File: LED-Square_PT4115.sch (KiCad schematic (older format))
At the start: 11 parts, among them U1 PT4115-SOT89-5

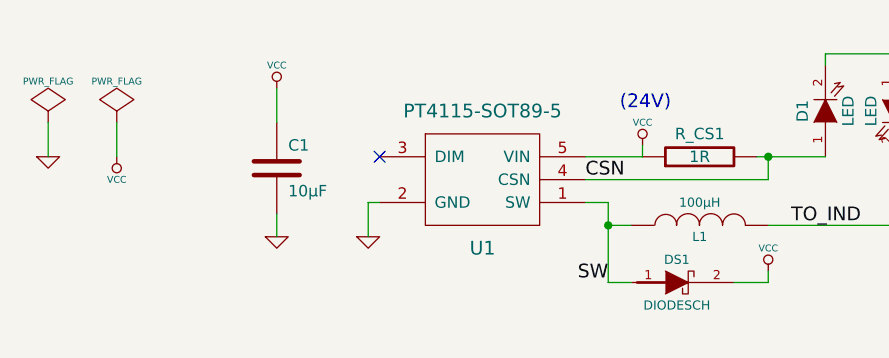
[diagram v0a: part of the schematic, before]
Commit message: Next step: add power connector(s) and maybe a pot for on-board dimming.
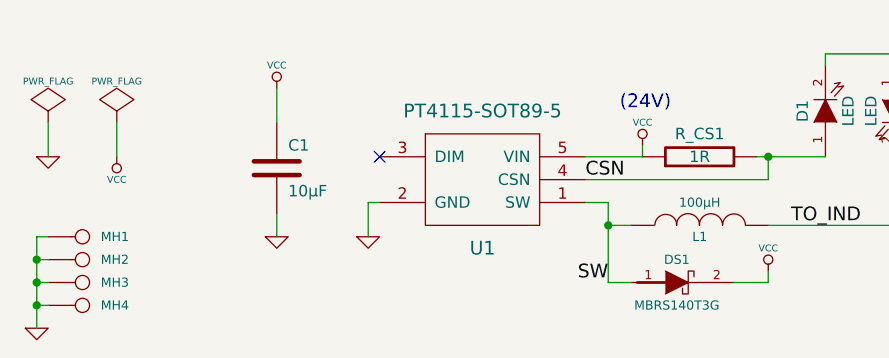
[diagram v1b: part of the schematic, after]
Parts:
- added MH1, MH2, MH3, MH4: CONN_1, symbol CONN_1
- DS1: value DIODESCH -> MBRS140T3G
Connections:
- net GND: now also MH1.1, MH2.1, MH3.1, MH4.1
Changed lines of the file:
@@
-EESchema Schematic File Version 2  date Fri 05 Oct 2012 10:36:36 PM CEST
+EESchema Schematic File Version 2  date Sat 06 Oct 2012 01:17:32 AM CEST
 LIBS:my_parts
 LIBS:power
@@
 Comment4 ""
 $EndDescr
-NoConn ~ 3100 2200
+$Comp
+L GND #PWR01
+U 1 1 506F6245
+P 1600 2950
+F 0 "#PWR01" H 1600 2950 30  0001 C CNN
+F 1 "GND" H 1600 2880 30  0001 C CNN
+	1    1600 2950
+	1    0    0    -1
+$EndComp
+Connection ~ 1600 2850
+Wire Wire Line
+	1600 2950 1600 2550
+Connection ~ 1600 2650
+Wire Wire Line
+	1600 2650 1650 2650
 Wire Wire Line
 	1950 2050 1950 2200
@@
 Wire Wire Line
 	1650 2050 1650 2200
+Wire Wire Line
+	1600 2850 1650 2850
+Wire Wire Line
+	1600 2550 1650 2550
+Wire Wire Line
+	1600 2750 1650 2750
+Connection ~ 1600 2750
+$Comp
+L CONN_1 MH4
+U 1 1 506F6221
+P 1800 2850
+F 0 "MH4" H 1880 2850 40  0000 L CNN
+F 1 "CONN_1" H 1800 2905 30  0001 C CNN
+	1    1800 2850
+	1    0    0    -1
+$EndComp
+$Comp
+L CONN_1 MH3
+U 1 1 506F621F
+P 1800 2750
+F 0 "MH3" H 1880 2750 40  0000 L CNN
+F 1 "CONN_1" H 1800 2805 30  0001 C CNN
+	1    1800 2750
+	1    0    0    -1
+$EndComp
+$Comp
+L CONN_1 MH2
+U 1 1 506F621C
+P 1800 2650
+F 0 "MH2" H 1880 2650 40  0000 L CNN
+F 1 "CONN_1" H 1800 2705 30  0001 C CNN
+	1    1800 2650
+	1    0    0    -1
+$EndComp
+$Comp
+L CONN_1 MH1
+U 1 1 506F6219
+P 1800 2550
+F 0 "MH1" H 1880 2550 40  0000 L CNN
+F 1 "CONN_1" H 1800 2605 30  0001 C CNN
+	1    1800 2550
+	1    0    0    -1
+$EndComp
+NoConn ~ 3100 2200
 Text Label 4900 2500 0    60   ~ 0
 TO_IND
@@
 White LEDs
 $Comp
-L VCC #PWR01
+L VCC #PWR02
 U 1 1 506F3B94
 P 1950 2200
-F 0 "#PWR01" H 1950 2300 30  0001 C CNN
+F 0 "#PWR02" H 1950 2300 30  0001 C CNN
 F 1 "VCC" H 1950 2300 30  0000 C CNN
 	1    1950 2200
@@
 $EndComp
 $Comp
-L GND #PWR02
+L GND #PWR03
 U 1 1 506F3B90
 P 1650 2200
-F 0 "#PWR02" H 1650 2200 30  0001 C CNN
+F 0 "#PWR03" H 1650 2200 30  0001 C CNN
 F 1 "GND" H 1650 2130 30  0001 C CNN
 	1    1650 2200
@@
 $EndComp
 $Comp
-L PWR_FLAG #FLG03
+L PWR_FLAG #FLG04
 U 1 1 506F3B8B
 P 1950 2050
-F 0 "#FLG03" H 1950 2145 30  0001 C CNN
+F 0 "#FLG04" H 1950 2145 30  0001 C CNN
 F 1 "PWR_FLAG" H 1950 2230 30  0000 C CNN
 	1    1950 2050
@@
 $EndComp
 $Comp
-L PWR_FLAG #FLG04
+L PWR_FLAG #FLG05
 U 1 1 506F3B82
 P 1650 2050
-F 0 "#FLG04" H 1650 2145 30  0001 C CNN
+F 0 "#FLG05" H 1650 2145 30  0001 C CNN
 F 1 "PWR_FLAG" H 1650 2230 30  0000 C CNN
 	1    1650 2050
@@
 $EndComp
 $Comp
-L VCC #PWR05
+L VCC #PWR06
 U 1 1 506F3B33
 P 4800 2700
-F 0 "#PWR05" H 4800 2800 30  0001 C CNN
+F 0 "#PWR06" H 4800 2800 30  0001 C CNN
 F 1 "VCC" H 4800 2800 30  0000 C CNN
 	1    4800 2700
@@
 $EndComp
 $Comp
-L VCC #PWR06
+L VCC #PWR07
 U 1 1 506F3A4D
 P 2650 1900
-F 0 "#PWR06" H 2650 2000 30  0001 C CNN
+F 0 "#PWR07" H 2650 2000 30  0001 C CNN
 F 1 "VCC" H 2650 2000 30  0000 C CNN
 	1    2650 1900
@@
 $EndComp
 $Comp
-L GND #PWR07
+L GND #PWR08
 U 1 1 506F3A48
 P 2650 2550
-F 0 "#PWR07" H 2650 2550 30  0001 C CNN
+F 0 "#PWR08" H 2650 2550 30  0001 C CNN
 F 1 "GND" H 2650 2480 30  0001 C CNN
 	1    2650 2550
@@
 $EndComp
 $Comp
-L VCC #PWR08
+L VCC #PWR09
 U 1 1 506F3A0F
 P 4250 2150
-F 0 "#PWR08" H 4250 2250 30  0001 C CNN
+F 0 "#PWR09" H 4250 2250 30  0001 C CNN
 F 1 "VCC" H 4250 2250 30  0000 C CNN
 	1    4250 2150
@@
 $EndComp
 $Comp
-L GND #PWR09
+L GND #PWR010
 U 1 1 506F39FF
 P 3050 2550
-F 0 "#PWR09" H 3050 2550 30  0001 C CNN
+F 0 "#PWR010" H 3050 2550 30  0001 C CNN
 F 1 "GND" H 3050 2480 30  0001 C CNN
 	1    3050 2550
@@
 P 4400 2750
 F 0 "DS1" H 4400 2850 40  0000 C CNN
-F 1 "DIODESCH" H 4400 2650 40  0000 C CNN
+F 1 "MBRS140T3G" H 4400 2650 40  0000 C CNN
 	1    4400 2750
 	1    0    0    -1

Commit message: Added copper pour as LED heatsinks.
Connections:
- net D1HS: now reaches D1.2 (K), D2.1 (A)
- net D2HS: now reaches D2.2 (K), D3.1 (A)
- net D3HS: now reaches D3.2 (K), D4.1 (A)
- net D4HS: now reaches D4.2 (K), D5.1 (A)
- net D5HS: now reaches D5.2 (K), D6.1 (A)
- net TO_IND renamed D6HS
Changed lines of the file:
@@
-EESchema Schematic File Version 2  date Sat 06 Oct 2012 01:17:32 AM CEST
+EESchema Schematic File Version 2  date Sat 06 Oct 2012 12:05:23 PM CEST
 LIBS:my_parts
 LIBS:power
@@
 Sheet 1 1
 Title "LED-Square PT4115"
-Date "5 oct 2012"
+Date "6 oct 2012"
 Rev "0.10"
 Comp "2012 - blog.spitzenpfeil.org"
@@
 Comment4 ""
 $EndDescr
+Text Label 6550 2250 2    60   ~ 0
+D6HS
+Text Label 6250 1750 2    60   ~ 0
+D5HS
+Text Label 5950 2250 2    60   ~ 0
+D4HS
+Text Label 5650 1750 2    60   ~ 0
+D3HS
+Text Label 5350 2250 2    60   ~ 0
+D2HS
+Text Label 5050 1750 2    60   ~ 0
+D1HS
 $Comp
 L GND #PWR01
@@
 $EndComp
 NoConn ~ 3100 2200
-Text Label 4900 2500 0    60   ~ 0
-TO_IND
 Text Label 4000 2300 0    60   ~ 0
 CSN
@@
 Text Notes 4150 2000 0    60   ~ 0
 (24V)
-Text Notes 5600 1700 0    60   ~ 0
+Text Notes 5550 1600 0    60   ~ 0
 White LEDs
 $Comp

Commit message: Added board-to-board connectors.
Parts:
- added P1: IN, symbol CONN_6
- added P2: OUT, symbol CONN_6
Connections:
- net GND: now also P1.1, P1.2, P2.5, P2.6; no longer MH1.1, MH2.1, MH3.1, MH4.1
- net VCC: now also P1.3, P1.4, P2.3, P2.4
- net DIM: now reaches U1.3 (DIM)
- net DIM: now also P1.6, P2.1
- no-connect marks 1 -> 6
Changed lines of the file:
@@
-EESchema Schematic File Version 2  date Sat 06 Oct 2012 12:05:23 PM CEST
+EESchema Schematic File Version 2  date Mon 22 Oct 2012 06:20:21 PM CEST
 LIBS:my_parts
 LIBS:power
@@
 Sheet 1 1
 Title "LED-Square PT4115"
-Date "6 oct 2012"
+Date "22 oct 2012"
 Rev "0.10"
 Comp "2012 - blog.spitzenpfeil.org"
@@
 Comment4 ""
 $EndDescr
+Connection ~ 2550 3450
+Wire Wire Line
+	2550 3450 2550 3550
+Wire Wire Line
+	2550 3550 2500 3550
+Connection ~ 2550 3650
+Wire Wire Line
+	2550 3650 2550 3750
+Wire Wire Line
+	2550 3750 2500 3750
+Wire Wire Line
+	2500 3950 2600 3950
+Wire Wire Line
+	1400 3950 1500 3950
+Wire Wire Line
+	1500 3750 1450 3750
+Connection ~ 1450 3650
+Wire Wire Line
+	1450 3750 1450 3650
+Connection ~ 1450 3450
+Wire Wire Line
+	1450 3450 1450 3550
+Wire Wire Line
+	1450 3550 1500 3550
+Wire Wire Line
+	1950 2050 1950 2200
+Connection ~ 4100 2500
+Wire Wire Line
+	4200 2750 4100 2750
+Wire Wire Line
+	4100 2750 4100 2400
+Wire Wire Line
+	6550 2200 6550 2500
+Wire Wire Line
+	6550 2500 4800 2500
+Connection ~ 4800 2200
+Wire Wire Line
+	5050 2200 4750 2200
+Wire Wire Line
+	2650 1900 2650 2050
+Wire Wire Line
+	4250 2150 4250 2200
+Wire Wire Line
+	4250 2200 4000 2200
+Wire Wire Line
+	6550 1800 6550 1750
+Wire Wire Line
+	6550 1750 6250 1750
+Wire Wire Line
+	6250 1750 6250 1800
+Wire Wire Line
+	5950 1800 5950 1750
+Wire Wire Line
+	5950 1750 5650 1750
+Wire Wire Line
+	5650 1750 5650 1800
+Wire Wire Line
+	5350 1800 5350 1750
+Wire Wire Line
+	5350 1750 5050 1750
+Wire Wire Line
+	5050 1750 5050 1800
+Wire Wire Line
+	5350 2200 5350 2250
+Wire Wire Line
+	5350 2250 5650 2250
+Wire Wire Line
+	5650 2250 5650 2200
+Wire Wire Line
+	5950 2200 5950 2250
+Wire Wire Line
+	5950 2250 6250 2250
+Wire Wire Line
+	6250 2250 6250 2200
+Wire Wire Line
+	3100 2400 3050 2400
+Wire Wire Line
+	3050 2400 3050 2550
+Wire Wire Line
+	4000 2300 4800 2300
+Wire Wire Line
+	4800 2300 4800 2200
+Wire Wire Line
+	2650 2450 2650 2550
+Wire Wire Line
+	4100 2400 4000 2400
+Wire Wire Line
+	4100 2500 4200 2500
+Wire Wire Line
+	4650 2750 4800 2750
+Wire Wire Line
+	4800 2750 4800 2700
+Wire Wire Line
+	1650 2050 1650 2200
+Wire Wire Line
+	1250 3500 1250 3450
+Wire Wire Line
+	1250 3450 1500 3450
+Wire Wire Line
+	1250 3700 1250 3650
+Wire Wire Line
+	1250 3650 1500 3650
+Wire Wire Line
+	3050 2200 3100 2200
+Wire Wire Line
+	2500 3650 2750 3650
+Wire Wire Line
+	2750 3650 2750 3700
+Wire Wire Line
+	2500 3450 2750 3450
+Wire Wire Line
+	2750 3450 2750 3500
+NoConn ~ 2500 3850
+NoConn ~ 1500 3850
+Text Label 2600 3950 0    60   ~ 0
+DIM
+Text Label 1400 3950 2    60   ~ 0
+DIM
+Text Label 3050 2200 2    60   ~ 0
+DIM
+$Comp
+L VCC #PWR?
+U 1 1 5085715F
+P 2750 3700
+F 0 "#PWR?" H 2750 3800 30  0001 C CNN
+F 1 "VCC" H 2750 3800 30  0000 C CNN
+	1    2750 3700
+	-1   0    0    1
+$EndComp
+$Comp
+L VCC #PWR?
+U 1 1 5085714E
+P 1250 3700
+F 0 "#PWR?" H 1250 3800 30  0001 C CNN
+F 1 "VCC" H 1250 3800 30  0000 C CNN
+	1    1250 3700
+	-1   0    0    1
+$EndComp
+$Comp
+L GND #PWR?
+U 1 1 50857132
+P 2750 3500
+F 0 "#PWR?" H 2750 3500 30  0001 C CNN
+F 1 "GND" H 2750 3430 30  0001 C CNN
+	1    2750 3500
+	1    0    0    -1
+$EndComp
+$Comp
+L GND #PWR?
+U 1 1 50857116
+P 1250 3500
+F 0 "#PWR?" H 1250 3500 30  0001 C CNN
+F 1 "GND" H 1250 3430 30  0001 C CNN
+	1    1250 3500
+	1    0    0    -1
+$EndComp
+$Comp
+L CONN_6 P2
+U 1 1 508570CC
+P 2150 3700
+F 0 "P2" V 2100 3700 60  0000 C CNN
+F 1 "OUT" V 2200 3700 60  0000 C CNN
+	1    2150 3700
+	-1   0    0    1
+$EndComp
+$Comp
+L CONN_6 P1
+U 1 1 508570C8
+P 1850 3700
+F 0 "P1" V 1800 3700 60  0000 C CNN
+F 1 "IN" V 1900 3700 60  0000 C CNN
+	1    1850 3700
+	1    0    0    -1
+$EndComp
+NoConn ~ 1650 2850
+NoConn ~ 1650 2750
+NoConn ~ 1650 2650
+NoConn ~ 1650 2550
 Text Label 6550 2250 2    60   ~ 0
 D6HS
@@
 D1HS
 $Comp
-L GND #PWR01
-U 1 1 506F6245
-P 1600 2950
-F 0 "#PWR01" H 1600 2950 30  0001 C CNN
-F 1 "GND" H 1600 2880 30  0001 C CNN
-	1    1600 2950
-	1    0    0    -1
-$EndComp
-Connection ~ 1600 2850
-Wire Wire Line
-	1600 2950 1600 2550
-Connection ~ 1600 2650
-Wire Wire Line
-	1600 2650 1650 2650
-Wire Wire Line
-	1950 2050 1950 2200
-Connection ~ 4100 2500
-Wire Wire Line
-	4200 2750 4100 2750
-Wire Wire Line
-	4100 2750 4100 2400
-Wire Wire Line
-	6550 2200 6550 2500
-Wire Wire Line
-	6550 2500 4800 2500
-Connection ~ 4800 2200
-Wire Wire Line
-	5050 2200 4750 2200
-Wire Wire Line
-	2650 1900 2650 2050
-Wire Wire Line
-	4250 2150 4250 2200
-Wire Wire Line
-	4250 2200 4000 2200
-Wire Wire Line
-	6550 1800 6550 1750
-Wire Wire Line
-	6550 1750 6250 1750
-Wire Wire Line
-	6250 1750 6250 1800
-Wire Wire Line
-	5950 1800 5950 1750
-Wire Wire Line
-	5950 1750 5650 1750
-Wire Wire Line
-	5650 1750 5650 1800
-Wire Wire Line
-	5350 1800 5350 1750
-Wire Wire Line
-	5350 1750 5050 1750
-Wire Wire Line
-	5050 1750 5050 1800
-Wire Wire Line
-	5350 2200 5350 2250
-Wire Wire Line
-	5350 2250 5650 2250
-Wire Wire Line
-	5650 2250 5650 2200
-Wire Wire Line
-	5950 2200 5950 2250
-Wire Wire Line
-	5950 2250 6250 2250
-Wire Wire Line
-	6250 2250 6250 2200
-Wire Wire Line
-	3100 2400 3050 2400
-Wire Wire Line
-	3050 2400 3050 2550
-Wire Wire Line
-	4000 2300 4800 2300
-Wire Wire Line
-	4800 2300 4800 2200
-Wire Wire Line
-	2650 2450 2650 2550
-Wire Wire Line
-	4100 2400 4000 2400
-Wire Wire Line
-	4100 2500 4200 2500
-Wire Wire Line
-	4650 2750 4800 2750
-Wire Wire Line
-	4800 2750 4800 2700
-Wire Wire Line
-	1650 2050 1650 2200
-Wire Wire Line
-	1600 2850 1650 2850
-Wire Wire Line
-	1600 2550 1650 2550
-Wire Wire Line
-	1600 2750 1650 2750
-Connection ~ 1600 2750
-$Comp
 L CONN_1 MH4
 U 1 1 506F6221
@@
 	1    0    0    -1
 $EndComp
-NoConn ~ 3100 2200
 Text Label 4000 2300 0    60   ~ 0
 CSN

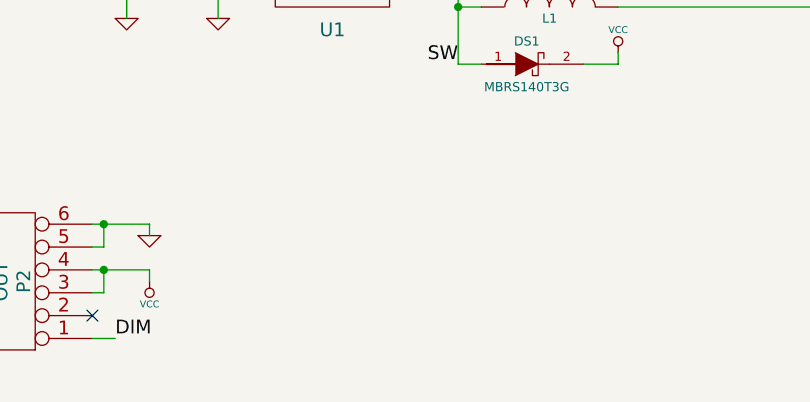
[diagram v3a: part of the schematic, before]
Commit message: Added a few more caps on the supply rail.
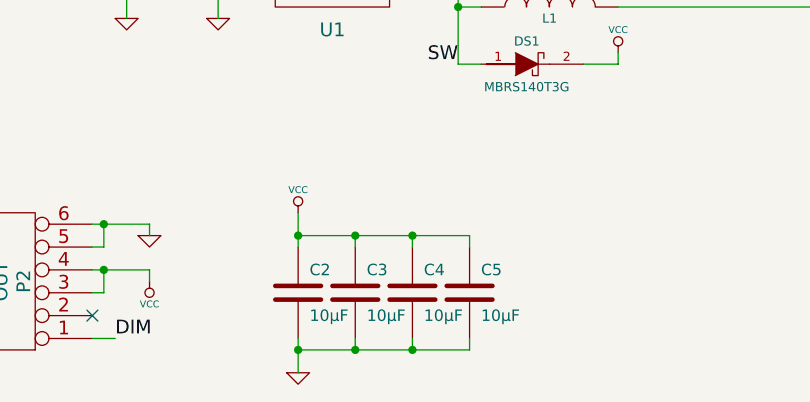
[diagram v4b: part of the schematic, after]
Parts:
- added C2, C3, C4, C5: 10µF, symbol C
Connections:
- net GND: now also C2.2, C3.2, C4.2, C5.2
- net VCC: now also C2.1, C3.1, C4.1, C5.1
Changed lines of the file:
@@
-EESchema Schematic File Version 2  date Mon 22 Oct 2012 06:20:21 PM CEST
+EESchema Schematic File Version 2  date Wed 24 Oct 2012 06:42:53 AM CEST
 LIBS:my_parts
 LIBS:power
@@
 Sheet 1 1
 Title "LED-Square PT4115"
-Date "22 oct 2012"
+Date "24 oct 2012"
 Rev "0.10"
 Comp "2012 - blog.spitzenpfeil.org"
@@
 Comment4 ""
 $EndDescr
+$Comp
+L VCC #PWR01
+U 1 1 508771C2
+P 3400 3400
+F 0 "#PWR01" H 3400 3500 30  0001 C CNN
+F 1 "VCC" H 3400 3500 30  0000 C CNN
+	1    3400 3400
+	1    0    0    -1
+$EndComp
+$Comp
+L GND #PWR02
+U 1 1 508771BD
+P 3400 4100
+F 0 "#PWR02" H 3400 4100 30  0001 C CNN
+F 1 "GND" H 3400 4030 30  0001 C CNN
+	1    3400 4100
+	1    0    0    -1
+$EndComp
+Connection ~ 3400 3500
+Wire Wire Line
+	3400 3400 3400 3550
+Connection ~ 3650 4000
+Wire Wire Line
+	3650 3950 3650 4000
+Wire Wire Line
+	4150 3950 4150 4000
+Wire Wire Line
+	4150 4000 3400 4000
+Connection ~ 3900 3500
+Wire Wire Line
+	3900 3550 3900 3500
 Connection ~ 2550 3450
 Wire Wire Line
@@
 Wire Wire Line
 	2750 3450 2750 3500
+Wire Wire Line
+	3400 3500 4150 3500
+Wire Wire Line
+	4150 3500 4150 3550
+Wire Wire Line
+	3650 3550 3650 3500
+Connection ~ 3650 3500
+Wire Wire Line
+	3900 3950 3900 4000
+Connection ~ 3900 4000
+Wire Wire Line
+	3400 4100 3400 3950
+Connection ~ 3400 4000
+$Comp
+L C C5
+U 1 1 50877174
+P 4150 3750
+F 0 "C5" H 4200 3850 50  0000 L CNN
+F 1 "10µF" H 4200 3650 50  0000 L CNN
+	1    4150 3750
+	1    0    0    -1
+$EndComp
+$Comp
+L C C4
+U 1 1 50877171
+P 3900 3750
+F 0 "C4" H 3950 3850 50  0000 L CNN
+F 1 "10µF" H 3950 3650 50  0000 L CNN
+	1    3900 3750
+	1    0    0    -1
+$EndComp
+$Comp
+L C C3
+U 1 1 5087716E
+P 3650 3750
+F 0 "C3" H 3700 3850 50  0000 L CNN
+F 1 "10µF" H 3700 3650 50  0000 L CNN
+	1    3650 3750
+	1    0    0    -1
+$EndComp
+$Comp
+L C C2
+U 1 1 50877166
+P 3400 3750
+F 0 "C2" H 3450 3850 50  0000 L CNN
+F 1 "10µF" H 3450 3650 50  0000 L CNN
+	1    3400 3750
+	1    0    0    -1
+$EndComp
 NoConn ~ 2500 3850
 NoConn ~ 1500 3850
@@
 DIM
 $Comp
-L VCC #PWR?
+L VCC #PWR03
 U 1 1 5085715F
 P 2750 3700
-F 0 "#PWR?" H 2750 3800 30  0001 C CNN
+F 0 "#PWR03" H 2750 3800 30  0001 C CNN
 F 1 "VCC" H 2750 3800 30  0000 C CNN
 	1    2750 3700
@@
 $EndComp
 $Comp
-L VCC #PWR?
+L VCC #PWR04
 U 1 1 5085714E
 P 1250 3700
-F 0 "#PWR?" H 1250 3800 30  0001 C CNN
+F 0 "#PWR04" H 1250 3800 30  0001 C CNN
 F 1 "VCC" H 1250 3800 30  0000 C CNN
 	1    1250 3700
@@
 $EndComp
 $Comp
-L GND #PWR?
+L GND #PWR05
 U 1 1 50857132
 P 2750 3500
-F 0 "#PWR?" H 2750 3500 30  0001 C CNN
+F 0 "#PWR05" H 2750 3500 30  0001 C CNN
 F 1 "GND" H 2750 3430 30  0001 C CNN
 	1    2750 3500
@@
 $EndComp
 $Comp
-L GND #PWR?
+L GND #PWR06
 U 1 1 50857116
 P 1250 3500
-F 0 "#PWR?" H 1250 3500 30  0001 C CNN
+F 0 "#PWR06" H 1250 3500 30  0001 C CNN
 F 1 "GND" H 1250 3430 30  0001 C CNN
 	1    1250 3500
@@
 White LEDs
 $Comp
-L VCC #PWR02
+L VCC #PWR07
 U 1 1 506F3B94
 P 1950 2200
-F 0 "#PWR02" H 1950 2300 30  0001 C CNN
+F 0 "#PWR07" H 1950 2300 30  0001 C CNN
 F 1 "VCC" H 1950 2300 30  0000 C CNN
 	1    1950 2200
@@
 $EndComp
 $Comp
-L GND #PWR03
+L GND #PWR08
 U 1 1 506F3B90
 P 1650 2200
-F 0 "#PWR03" H 1650 2200 30  0001 C CNN
+F 0 "#PWR08" H 1650 2200 30  0001 C CNN
 F 1 "GND" H 1650 2130 30  0001 C CNN
 	1    1650 2200
@@
 $EndComp
 $Comp
-L PWR_FLAG #FLG04
+L PWR_FLAG #FLG09
 U 1 1 506F3B8B
 P 1950 2050
-F 0 "#FLG04" H 1950 2145 30  0001 C CNN
+F 0 "#FLG09" H 1950 2145 30  0001 C CNN
 F 1 "PWR_FLAG" H 1950 2230 30  0000 C CNN
 	1    1950 2050
@@
 $EndComp
 $Comp
-L PWR_FLAG #FLG05
+L PWR_FLAG #FLG010
 U 1 1 506F3B82
 P 1650 2050
-F 0 "#FLG05" H 1650 2145 30  0001 C CNN
+F 0 "#FLG010" H 1650 2145 30  0001 C CNN
 F 1 "PWR_FLAG" H 1650 2230 30  0000 C CNN
 	1    1650 2050
@@
 $EndComp
 $Comp
-L VCC #PWR06
+L VCC #PWR011
 U 1 1 506F3B33
 P 4800 2700
-F 0 "#PWR06" H 4800 2800 30  0001 C CNN
+F 0 "#PWR011" H 4800 2800 30  0001 C CNN
 F 1 "VCC" H 4800 2800 30  0000 C CNN
 	1    4800 2700
@@
 $EndComp
 $Comp
-L VCC #PWR07
+L VCC #PWR012
 U 1 1 506F3A4D
 P 2650 1900
-F 0 "#PWR07" H 2650 2000 30  0001 C CNN
+F 0 "#PWR012" H 2650 2000 30  0001 C CNN
 F 1 "VCC" H 2650 2000 30  0000 C CNN
 	1    2650 1900
@@
 $EndComp
 $Comp
-L GND #PWR08
+L GND #PWR013
 U 1 1 506F3A48
 P 2650 2550
-F 0 "#PWR08" H 2650 2550 30  0001 C CNN
+F 0 "#PWR013" H 2650 2550 30  0001 C CNN
 F 1 "GND" H 2650 2480 30  0001 C CNN
 	1    2650 2550
@@
 $EndComp
 $Comp
-L VCC #PWR09
+L VCC #PWR014
 U 1 1 506F3A0F
 P 4250 2150
-F 0 "#PWR09" H 4250 2250 30  0001 C CNN
+F 0 "#PWR014" H 4250 2250 30  0001 C CNN
 F 1 "VCC" H 4250 2250 30  0000 C CNN
 	1    4250 2150
@@
 $EndComp
 $Comp
-L GND #PWR010
+L GND #PWR015
 U 1 1 506F39FF
 P 3050 2550
-F 0 "#PWR010" H 3050 2550 30  0001 C CNN
+F 0 "#PWR015" H 3050 2550 30  0001 C CNN
 F 1 "GND" H 3050 2480 30  0001 C CNN
 	1    3050 2550
